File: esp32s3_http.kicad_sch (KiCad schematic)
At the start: 39 parts, among them J1 USB_B, J2 Jack-DC, J3 UART0, SW1 SW_Push, SW2 SW_Push, U1 ESP32-S3-WROOM-1, U2 LM2940T-3.3, U3 NJM7805FA, Y1 32.768KHz

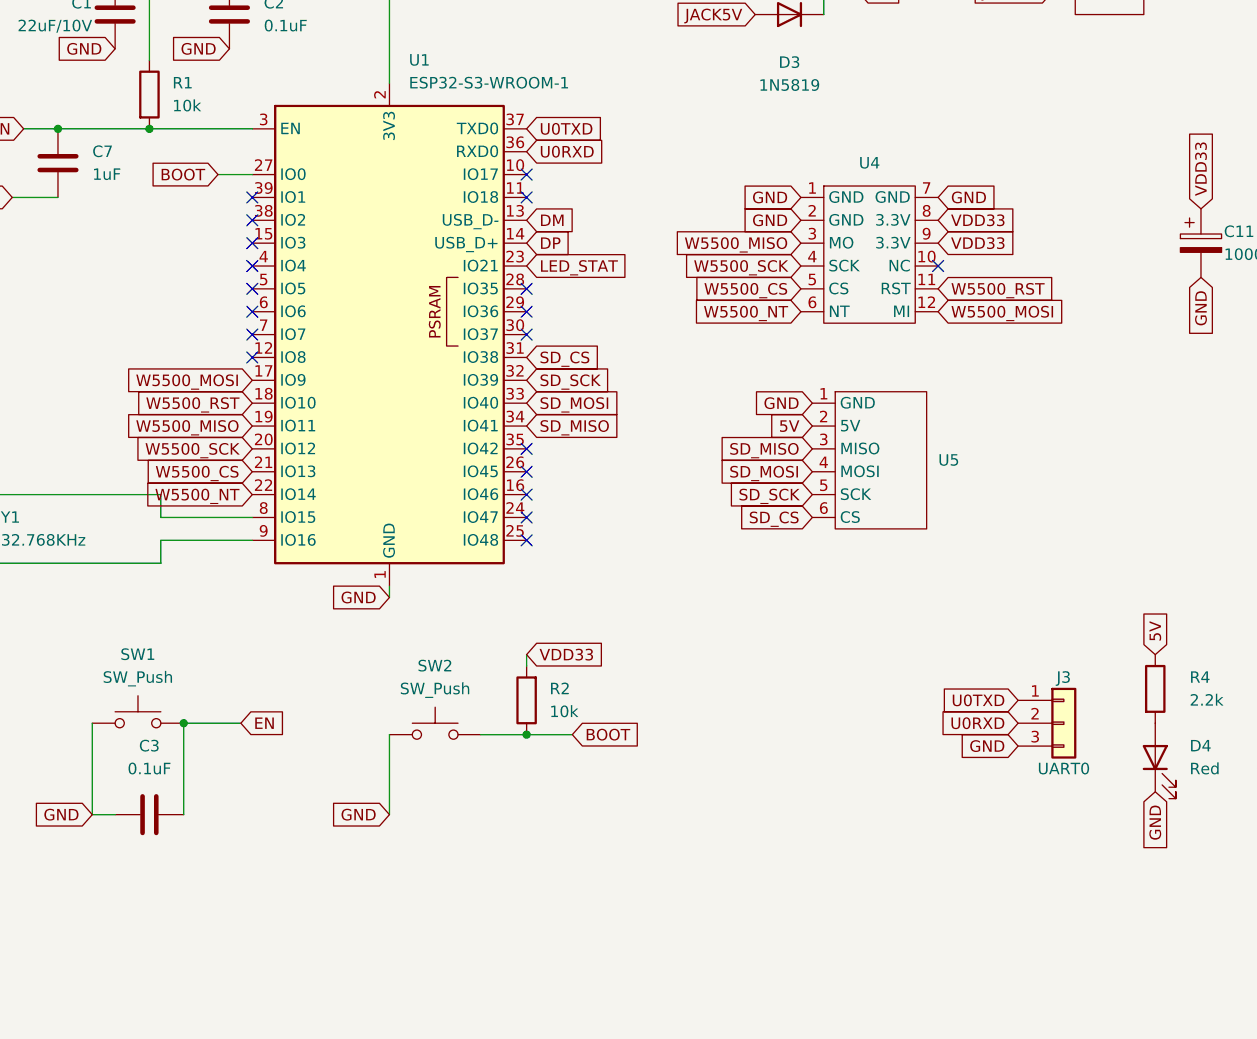
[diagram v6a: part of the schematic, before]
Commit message: 回路図: 空き GPIO をピンヘッダに引き出し
- J3 (2x4): UART0 TX/RX, IO1, IO2, IO42, IO47, IO48, GND
- J4 (2x6): 5V, 3V3, GND x2, IO3-IO8, IO17, IO18
- IO45/IO46 (ストラッピング), IO35-37 (PSRAM), IO15/16 (32k 水晶) は除外

Co-Authored-By: Claude Opus 5.5 <noreply@anthropic.com>
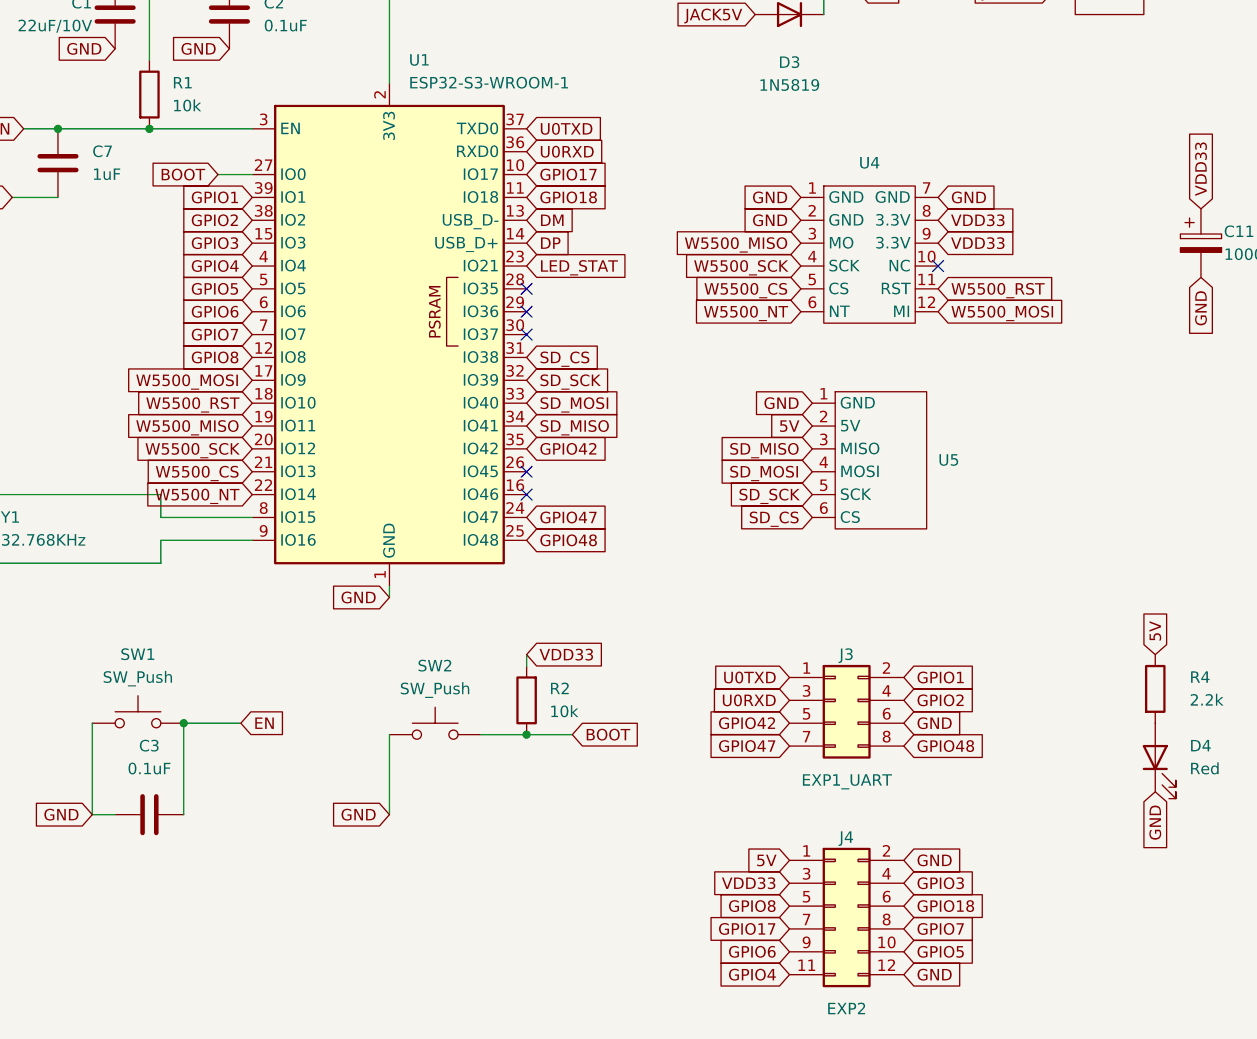
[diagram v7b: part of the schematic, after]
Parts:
- removed J3: UART0, Connector_PinHeader_2.54mm:PinHeader_1x03_P2.54mm_Vertical, symbol Connector_Generic:Conn_01x03
- added J3: EXP1_UART, Connector_PinHeader_2.54mm:PinHeader_2x04_P2.54mm_Vertical, symbol Connector_Generic:Conn_02x04_Odd_Even
- added J4: EXP2, Connector_PinHeader_2.54mm:PinHeader_2x06_P2.54mm_Vertical, symbol Connector_Generic:Conn_02x06_Odd_Even
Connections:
- net 5V: now also J4.1 (Pin_1)
- net GND: now also J3.6 (Pin_6), J4.12 (Pin_12), J4.2 (Pin_2)
- net U0RXD: now also J3.3 (Pin_3)
- net U0TXD: now also J3.1 (Pin_1)
- net VDD33: now also J4.3 (Pin_3)
- net GPIO17: now reaches U1.10 (IO17)
- net GPIO17: now also J4.7 (Pin_7)
- net GPIO18: now reaches U1.11 (IO18)
- net GPIO18: now also J4.6 (Pin_6)
- net GPIO8: now reaches U1.12 (IO8)
- net GPIO8: now also J4.5 (Pin_5)
- net GPIO3: now reaches U1.15 (IO3)
- net GPIO3: now also J4.4 (Pin_4)
- net GPIO47: now reaches U1.24 (IO47)
- net GPIO47: now also J3.7 (Pin_7)
- net GPIO48: now reaches U1.25 (IO48)
- net GPIO48: now also J3.8 (Pin_8)
- net GPIO42: now reaches U1.35 (IO42)
- net GPIO42: now also J3.5 (Pin_5)
- net GPIO2: now reaches U1.38 (IO2)
- net GPIO2: now also J3.4 (Pin_4)
- net GPIO1: now reaches U1.39 (IO1)
- net GPIO1: now also J3.2 (Pin_2)
- net GPIO4: now reaches U1.4 (IO4)
- net GPIO4: now also J4.11 (Pin_11)
- net GPIO5: now reaches U1.5 (IO5)
- net GPIO5: now also J4.10 (Pin_10)
- net GPIO6: now reaches U1.6 (IO6)
- net GPIO6: now also J4.9 (Pin_9)
- net GPIO7: now reaches U1.7 (IO7)
- net GPIO7: now also J4.8 (Pin_8)
- no-connect marks 19 -> 6

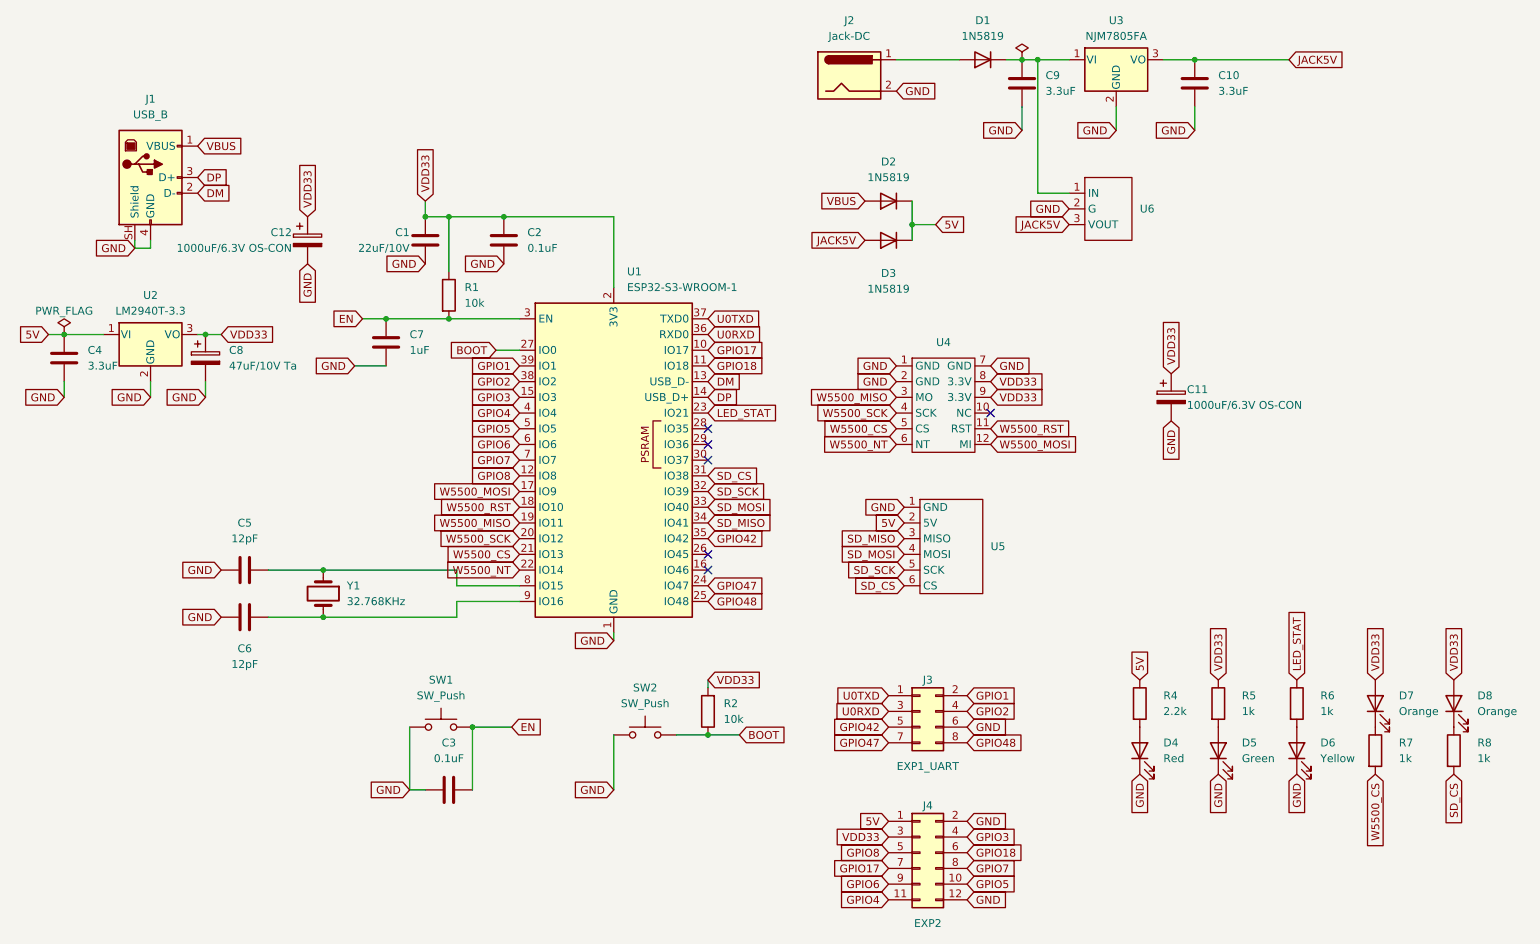
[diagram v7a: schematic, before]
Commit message: 回路図: 部品値を秋月の調達品に合わせる
- C8 47uF -> 22uF Ta, C4/C10 3.3uF -> 4.7uF, C9 3.3uF -> 1uF/25V
- C5/C6 12pF -> 15pF, R4 2.2k -> 1k

Co-Authored-By: Claude Opus 5.5 <noreply@anthropic.com>
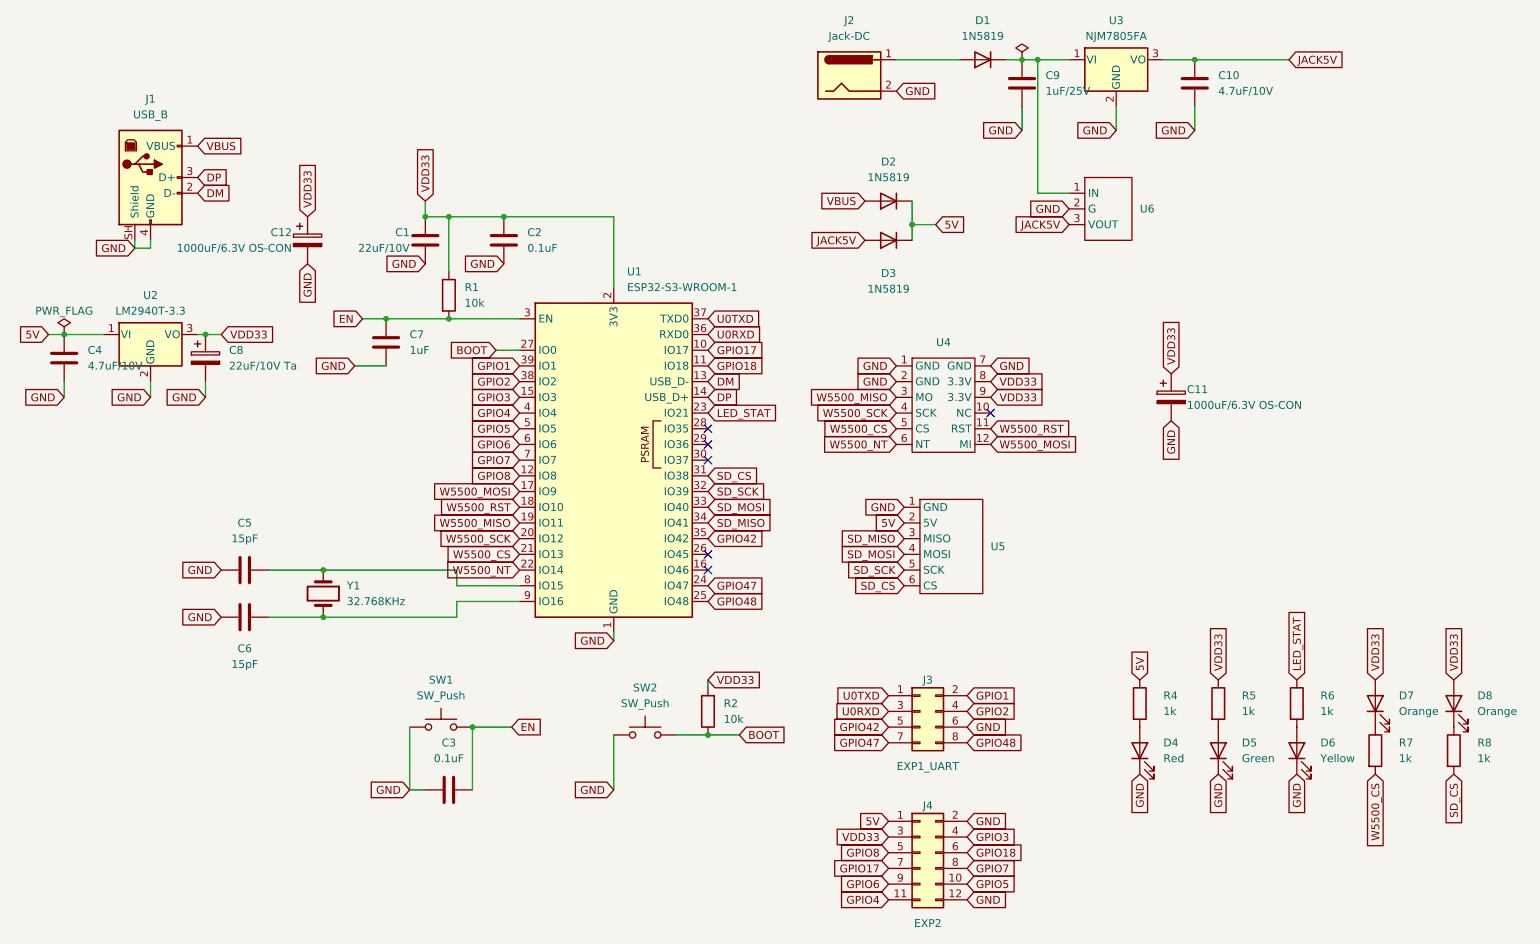
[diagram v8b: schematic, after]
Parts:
- C10, C4: value 3.3uF -> 4.7uF/10V
- C5, C6: value 12pF -> 15pF
- C8: value 47uF/10V Ta -> 22uF/10V Ta
- C9: value 3.3uF -> 1uF/25V
- R4: value 2.2k -> 1k
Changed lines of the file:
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@@
 			)
 		)
-		(property "Value" "3.3uF"
+		(property "Value" "4.7uF/10V"
 			(at 30.48 76.1999 0)
 			(show_name no)
@@
 			)
 		)
-		(property "Value" "3.3uF"
+		(property "Value" "1uF/25V"
 			(at 185.42 31.7499 0)
 			(show_name no)
@@
 			)
 		)
-		(property "Value" "12pF"
+		(property "Value" "15pF"
 			(at 55.88 124.46 90)
 			(show_name no)
@@
 			)
 		)
-		(property "Value" "3.3uF"
+		(property "Value" "4.7uF/10V"
 			(at 213.36 31.7499 0)
 			(show_name no)
@@
 			)
 		)
-		(property "Value" "47uF/10V Ta"
+		(property "Value" "22uF/10V Ta"
 			(at 53.34 76.2 0)
 			(show_name no)
@@
 			)
 		)
-		(property "Value" "12pF"
+		(property "Value" "15pF"
 			(at 55.88 104.14 90)
 			(show_name no)
@@
 			)
 		)
-		(property "Value" "2.2k"
+		(property "Value" "1k"
 			(at 204.47 132.08 0)
 			(show_name no)
